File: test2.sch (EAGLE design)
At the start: 15 parts, among them U1_1 2.1MMJACKTHM, U1_5 TMP36

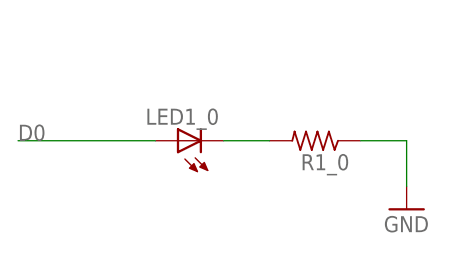
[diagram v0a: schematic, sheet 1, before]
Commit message: Lots of changes
Added catalog for Tantalum caps, LEDs

Added parent to HighEagle classes.  This required several things
   * Added base class to HighEagle classes (EaglFilePart)
   * started to move toward add_*() methods instead of inserting directly into collections.
   * Added a clone() function to perform deep copy because copy.deepcopy() will recurse up the parent pointers
   * parent has to be passed to from_et() 
   * all constructors take a parent

Lots of code to deal with layers.

Moved standard layers to NVSLLayers.lbr

Created library for symbols Symbols.lbr

Updated fixEagle.py to support normalizing layers.

Added base class for drawing element (DrawingElement)




git-svn-id: svn+ssh://bbfs-01.calit2.net/grw/Gordon/svn/trunk/Gadgets/Tools/CircuitsByCode@20023 2cf53259-273a-af40-bda6-69d31023b8ec
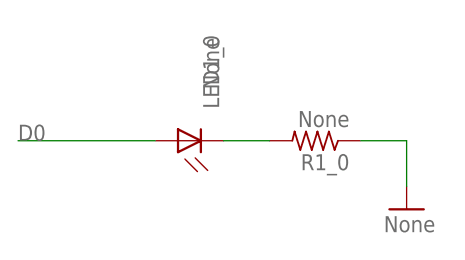
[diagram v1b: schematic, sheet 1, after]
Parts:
- LED1, LED1_3, LED1_4: value RGBLED_CA-5MM -> None
- LED1_0, R1_0: value (none) -> None
- U$2_2: value ARDUINO_MICRO_REV03J-BOB -> None
